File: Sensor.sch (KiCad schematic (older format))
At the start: 35 parts, among them U10 ACS722xLCTR-10AB, U11 AMC1100DWVR, U9 ACS722xLCTR-10AB

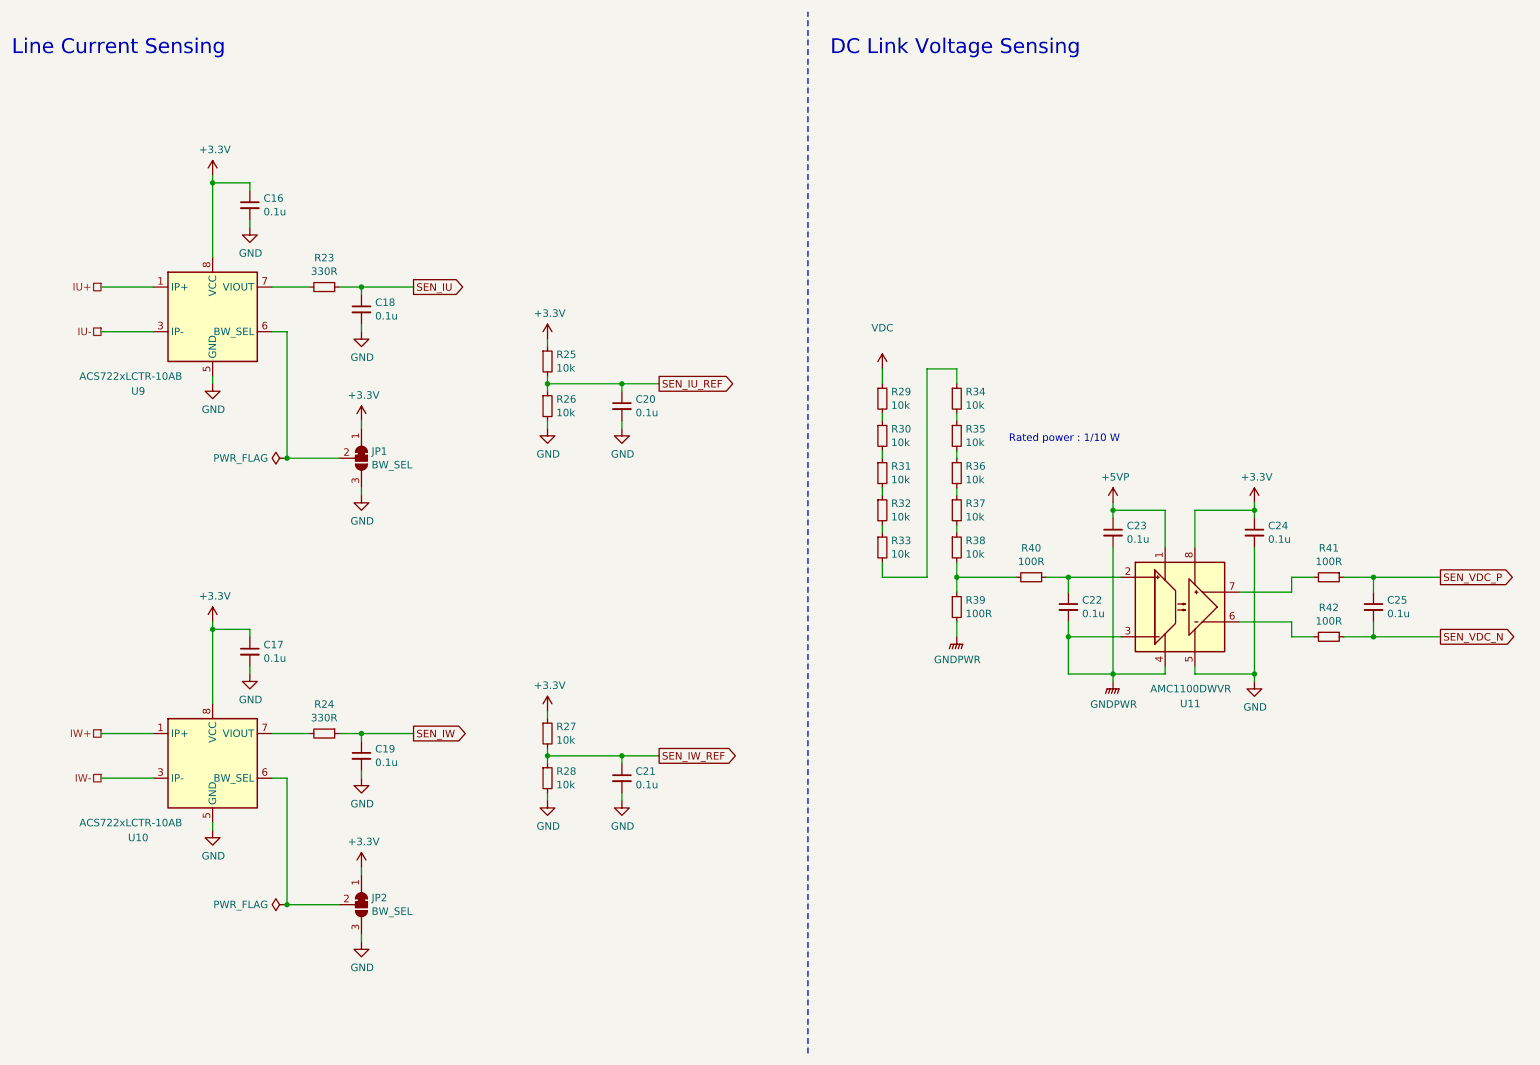
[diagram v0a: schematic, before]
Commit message: テストポイント追加，シルク調整，固定穴マスク追加
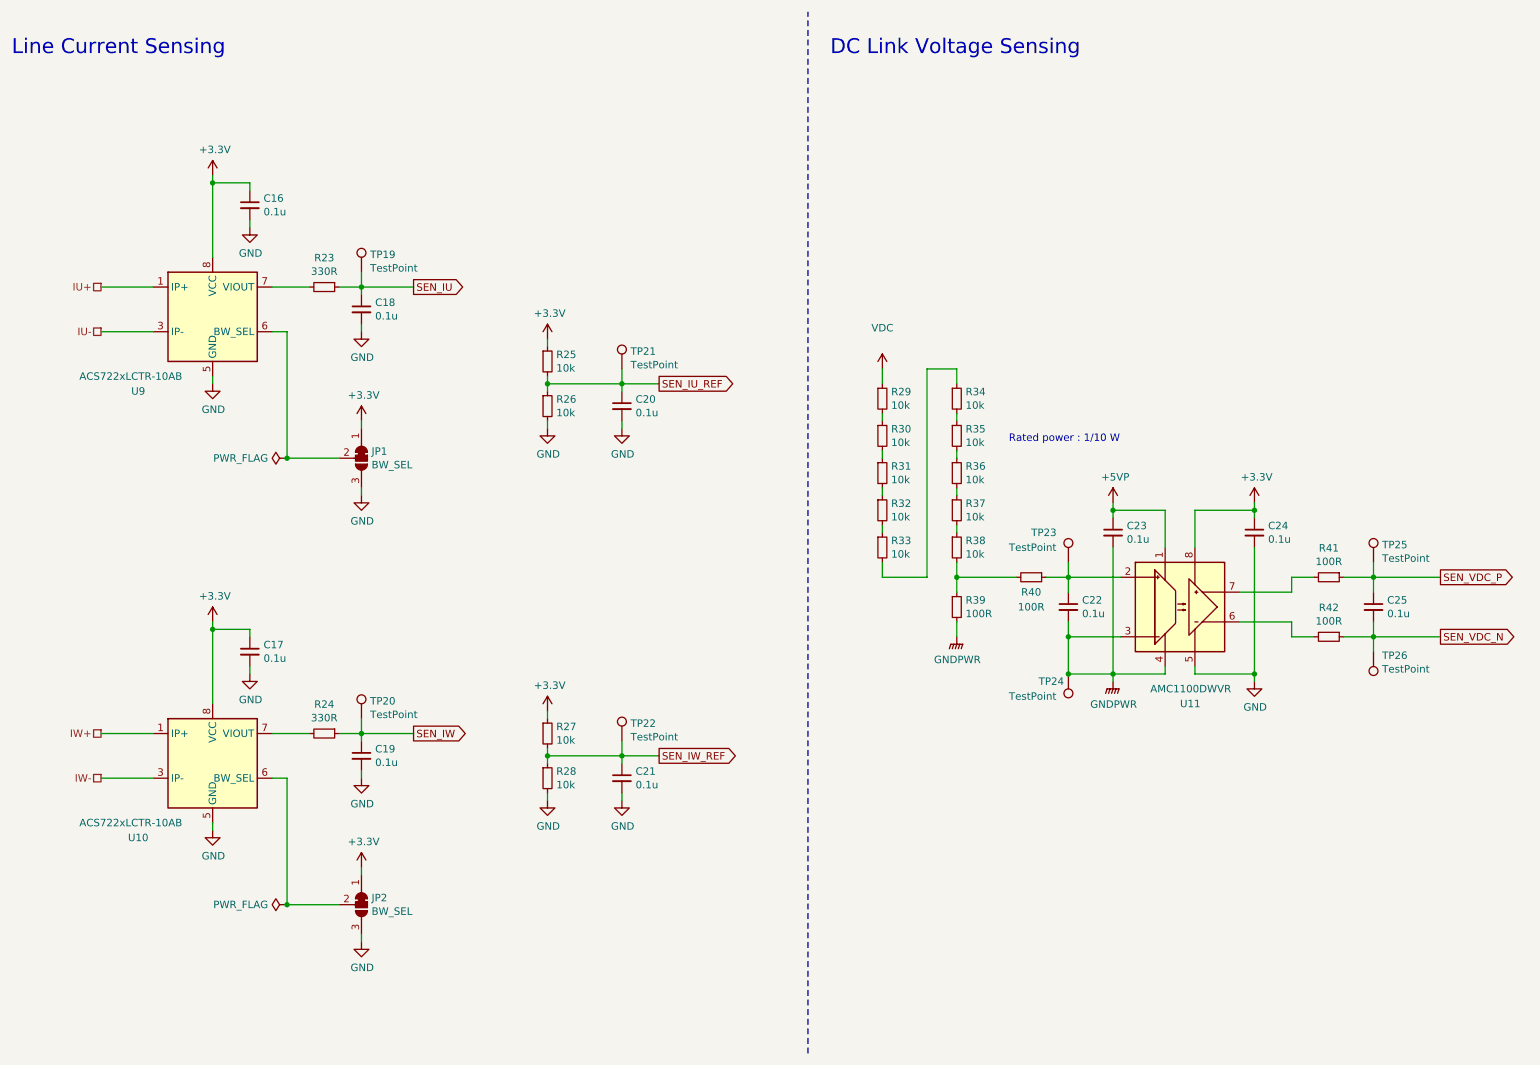
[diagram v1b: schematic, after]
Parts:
- added TP19, TP20, TP21, TP22, TP23, TP25, TP26: TestPoint, TestPoint:TestPoint_Pad_D1.0mm, symbol Connector:TestPoint
- added TP24: TestPoint, TestPoint:TestPoint_Loop_D2.50mm_Drill1.0mm_LowProfile, symbol Connector:TestPoint
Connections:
- net GNDPWR: now also TP24.1
- net SEN_IU: now also TP19.1
- net SEN_IU_REF: now also TP21.1
- net SEN_IW: now also TP20.1
- net SEN_IW_REF: now also TP22.1
- net SEN_VDC_N: now also TP26.1
- net SEN_VDC_P: now also TP25.1
- net at C22.1, R40.1, U11.2 (IN+): now also TP23.1
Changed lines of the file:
@@
 AR Path="/5E844691/5E89631E" Ref="R?"  Part="1"
 AR Path="/5E7F6C5B/5E89631E" Ref="R40"  Part="1"
-F 0 "R40" V 7304 4300 50  0000 C CNN
-F 1 "100R" V 7395 4300 50  0000 C CNN
+F 0 "R40" V 7600 4300 50  0000 C CNN
+F 1 "100R" V 7700 4300 50  0000 C CNN
 F 2 "Resistor_SMD:R_0603_1608Metric" H 7500 4300 50  0001 C CNN
 F 3 "~" H 7500 4300 50  0001 C CNN
@@
 $EndComp
 Connection ~ 2500 3500
+$Comp
+L Connector:TestPoint TP19
+U 1 1 5ECA6E64
+P 3000 2250
+F 0 "TP19" H 3058 2368 50  0000 L CNN
+F 1 "TestPoint" H 3058 2277 50  0000 L CNN
+F 2 "TestPoint:TestPoint_Pad_D1.0mm" H 3200 2250 50  0001 C CNN
+F 3 "~" H 3200 2250 50  0001 C CNN
+	1    3000 2250
+	1    0    0    -1
+$EndComp
+Wire Wire Line
+	3000 2250 3000 2350
+$Comp
+L Connector:TestPoint TP21
+U 1 1 5ECAA221
+P 4750 2900
+F 0 "TP21" H 4808 3018 50  0000 L CNN
+F 1 "TestPoint" H 4808 2927 50  0000 L CNN
+F 2 "TestPoint:TestPoint_Pad_D1.0mm" H 4950 2900 50  0001 C CNN
+F 3 "~" H 4950 2900 50  0001 C CNN
+	1    4750 2900
+	1    0    0    -1
+$EndComp
+Wire Wire Line
+	4750 2900 4750 3000
+$Comp
+L Connector:TestPoint TP20
+U 1 1 5ECAD965
+P 3000 5250
+F 0 "TP20" H 3058 5368 50  0000 L CNN
+F 1 "TestPoint" H 3058 5277 50  0000 L CNN
+F 2 "TestPoint:TestPoint_Pad_D1.0mm" H 3200 5250 50  0001 C CNN
+F 3 "~" H 3200 5250 50  0001 C CNN
+	1    3000 5250
+	1    0    0    -1
+$EndComp
+Wire Wire Line
+	3000 5250 3000 5350
+$Comp
+L Connector:TestPoint TP22
+U 1 1 5ECB1410
+P 4750 5400
+F 0 "TP22" H 4808 5518 50  0000 L CNN
+F 1 "TestPoint" H 4808 5427 50  0000 L CNN
+F 2 "TestPoint:TestPoint_Pad_D1.0mm" H 4950 5400 50  0001 C CNN
+F 3 "~" H 4950 5400 50  0001 C CNN
+	1    4750 5400
+	1    0    0    -1
+$EndComp
+Wire Wire Line
+	4750 5400 4750 5500
+$Comp
+L Connector:TestPoint TP25
+U 1 1 5ECB50EF
+P 9800 4200
+F 0 "TP25" H 9858 4318 50  0000 L CNN
+F 1 "TestPoint" H 9858 4227 50  0000 L CNN
+F 2 "TestPoint:TestPoint_Pad_D1.0mm" H 10000 4200 50  0001 C CNN
+F 3 "~" H 10000 4200 50  0001 C CNN
+	1    9800 4200
+	1    0    0    -1
+$EndComp
+Wire Wire Line
+	9800 4200 9800 4300
+$Comp
+L Connector:TestPoint TP26
+U 1 1 5ECB8C1D
+P 9800 4800
+F 0 "TP26" H 9742 4826 50  0000 R CNN
+F 1 "TestPoint" H 9742 4917 50  0000 R CNN
+F 2 "TestPoint:TestPoint_Pad_D1.0mm" H 10000 4800 50  0001 C CNN
+F 3 "~" H 10000 4800 50  0001 C CNN
+	1    9800 4800
+	-1   0    0    1
+$EndComp
+Wire Wire Line
+	9800 4800 9800 4700
+$Comp
+L Connector:TestPoint TP23
+U 1 1 5ECBD092
+P 7750 4200
+F 0 "TP23" H 7500 4400 50  0000 L CNN
+F 1 "TestPoint" H 7350 4300 50  0000 L CNN
+F 2 "TestPoint:TestPoint_Pad_D1.0mm" H 7950 4200 50  0001 C CNN
+F 3 "~" H 7950 4200 50  0001 C CNN
+	1    7750 4200
+	1    0    0    -1
+$EndComp
+Wire Wire Line
+	7750 4200 7750 4300
+$Comp
+L Connector:TestPoint TP24
+U 1 1 5ED3D113
+P 7750 4950
+F 0 "TP24" H 7950 5000 50  0000 R CNN
+F 1 "TestPoint" H 8150 5100 50  0000 R CNN
+F 2 "TestPoint:TestPoint_Loop_D2.50mm_Drill1.0mm_LowProfile" H 7950 4950 50  0001 C CNN
+F 3 "~" H 7950 4950 50  0001 C CNN
+	1    7750 4950
+	-1   0    0    1
+$EndComp
+Connection ~ 7750 4950
 $EndSCHEMATC
